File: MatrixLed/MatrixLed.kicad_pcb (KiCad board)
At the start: 2 copper layers, 0 parts

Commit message: Añadida serigrafia reflectante
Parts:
- added C1: 10uF, Capacitors_SMD:C_1206, B.Cu at (205.7, 72.1)
- added D1: LED_ALT, LEDs:LED_0603, F.Cu at (181.0, 59.7)
- added D10: LED_ALT, LEDs:LED_0603, F.Cu at (185.4, 62.9)
- added D11: LED_ALT, LEDs:LED_0603, F.Cu at (185.4, 66.0)
- added D12: LED_ALT, LEDs:LED_0603, F.Cu at (185.4, 69.2)
- added D13: LED_ALT, LEDs:LED_0603, F.Cu at (185.4, 72.4)
- added D14: LED_ALT, LEDs:LED_0603, F.Cu at (185.4, 75.6)
- added D15: LED_ALT, LEDs:LED_0603, F.Cu at (185.4, 78.7)
- added D16: LED_ALT, LEDs:LED_0603, F.Cu at (185.4, 81.9)
- added D17: LED_ALT, LEDs:LED_0603, F.Cu at (189.9, 59.7)
- added D18: LED_ALT, LEDs:LED_0603, F.Cu at (189.9, 62.9)
- added D19: LED_ALT, LEDs:LED_0603, F.Cu at (189.9, 66.0)
- added D2: LED_ALT, LEDs:LED_0603, F.Cu at (181.0, 62.9)
- added D20: LED_ALT, LEDs:LED_0603, F.Cu at (189.9, 69.2)
- added D21: LED_ALT, LEDs:LED_0603, F.Cu at (189.9, 72.4)
- added D22: LED_ALT, LEDs:LED_0603, F.Cu at (189.9, 75.6)
- added D23: LED_ALT, LEDs:LED_0603, F.Cu at (189.9, 78.7)
- added D24: LED_ALT, LEDs:LED_0603, F.Cu at (189.9, 81.9)
- added D25: LED_ALT, LEDs:LED_0603, F.Cu at (194.3, 59.7)
- added D26: LED_ALT, LEDs:LED_0603, F.Cu at (194.3, 62.9)
- added D27: LED_ALT, LEDs:LED_0603, F.Cu at (194.3, 66.0)
- added D28: LED_ALT, LEDs:LED_0603, F.Cu at (194.3, 69.2)
- added D29: LED_ALT, LEDs:LED_0603, F.Cu at (194.3, 72.4)
- added D3: LED_ALT, LEDs:LED_0603, F.Cu at (181.0, 66.0)
- added D30: LED_ALT, LEDs:LED_0603, F.Cu at (194.3, 75.6)
- added D31: LED_ALT, LEDs:LED_0603, F.Cu at (194.3, 78.7)
- added D32: LED_ALT, LEDs:LED_0603, F.Cu at (194.3, 81.9)
- added D33: LED_ALT, LEDs:LED_0603, F.Cu at (198.8, 59.7)
- added D34: LED_ALT, LEDs:LED_0603, F.Cu at (198.8, 62.9)
- added D35: LED_ALT, LEDs:LED_0603, F.Cu at (198.8, 66.0)
- added D36: LED_ALT, LEDs:LED_0603, F.Cu at (198.8, 69.2)
- added D37: LED_ALT, LEDs:LED_0603, F.Cu at (198.8, 72.4)
- added D38: LED_ALT, LEDs:LED_0603, F.Cu at (198.8, 75.6)
- added D39: LED_ALT, LEDs:LED_0603, F.Cu at (198.8, 78.7)
- added D4: LED_ALT, LEDs:LED_0603, F.Cu at (181.0, 69.2)
- added D40: LED_ALT, LEDs:LED_0603, F.Cu at (198.8, 81.9)
- added D41: LED_ALT, LEDs:LED_0603, F.Cu at (203.2, 59.7)
- added D42: LED_ALT, LEDs:LED_0603, F.Cu at (203.2, 62.9)
- added D43: LED_ALT, LEDs:LED_0603, F.Cu at (203.2, 66.0)
- added D44: LED_ALT, LEDs:LED_0603, F.Cu at (203.2, 69.2)
- added D45: LED_ALT, LEDs:LED_0603, F.Cu at (203.2, 72.4)
- added D46: LED_ALT, LEDs:LED_0603, F.Cu at (203.2, 75.6)
- added D47: LED_ALT, LEDs:LED_0603, F.Cu at (203.2, 78.7)
- added D48: LED_ALT, LEDs:LED_0603, F.Cu at (203.2, 81.9)
- added D49: LED_ALT, LEDs:LED_0603, F.Cu at (207.6, 59.7)
- added D5: LED_ALT, LEDs:LED_0603, F.Cu at (181.0, 72.4)
- added D50: LED_ALT, LEDs:LED_0603, F.Cu at (207.6, 62.9)
- added D51: LED_ALT, LEDs:LED_0603, F.Cu at (207.6, 66.0)
- added D52: LED_ALT, LEDs:LED_0603, F.Cu at (207.6, 69.2)
- added D53: LED_ALT, LEDs:LED_0603, F.Cu at (207.6, 72.4)
- added D54: LED_ALT, LEDs:LED_0603, F.Cu at (207.6, 75.6)
- added D55: LED_ALT, LEDs:LED_0603, F.Cu at (207.6, 78.7)
- added D56: LED_ALT, LEDs:LED_0603, F.Cu at (207.6, 81.9)
- added D57: LED_ALT, LEDs:LED_0603, F.Cu at (212.1, 59.7)
- added D58: LED_ALT, LEDs:LED_0603, F.Cu at (212.1, 62.9)
- added D59: LED_ALT, LEDs:LED_0603, F.Cu at (212.1, 66.0)
- added D6: LED_ALT, LEDs:LED_0603, F.Cu at (181.0, 75.6)
- added D60: LED_ALT, LEDs:LED_0603, F.Cu at (212.1, 69.2)
- added D61: LED_ALT, LEDs:LED_0603, F.Cu at (212.1, 72.4)
- added D62: LED_ALT, LEDs:LED_0603, F.Cu at (212.1, 75.6)
- added D63: LED_ALT, LEDs:LED_0603, F.Cu at (212.1, 78.7)
- added D64: LED_ALT, LEDs:LED_0603, F.Cu at (212.1, 81.9)
- added D65: 1N4148, Diodes_SMD:D_SOD-123, B.Cu at (202.5, 72.7)
- added D7: LED_ALT, LEDs:LED_0603, F.Cu at (181.0, 78.7)
- added D8: LED_ALT, LEDs:LED_0603, F.Cu at (181.0, 81.9)
- added D9: LED_ALT, LEDs:LED_0603, F.Cu at (185.4, 59.7)
- added G***: LOGO, logos_frizzy:cuadrado, F.Cu at (212.0, 81.9)
- added G***: LOGO, logos_frizzy:cuadrado, F.Cu at (207.5, 78.9)
- added G***: LOGO, logos_frizzy:cuadrado, F.Cu at (203.1, 78.9)
- added G***: LOGO, logos_frizzy:cuadrado, F.Cu at (198.6, 78.9)
- added G***: LOGO, logos_frizzy:cuadrado, F.Cu at (194.2, 78.9)
- added G***: LOGO, logos_frizzy:cuadrado, F.Cu at (189.7, 78.9)
- added G***: LOGO, logos_frizzy:cuadrado, F.Cu at (185.3, 78.9)
- added G***: LOGO, logos_frizzy:cuadrado, F.Cu at (180.8, 78.9)
- added G***: LOGO, logos_frizzy:cuadrado, F.Cu at (212.0, 75.7)
- added G***: LOGO, logos_frizzy:cuadrado, F.Cu at (207.5, 75.7)
- added G***: LOGO, logos_frizzy:cuadrado, F.Cu at (203.1, 75.7)
- added G***: LOGO, logos_frizzy:cuadrado, F.Cu at (207.5, 81.9)
- added G***: LOGO, logos_frizzy:cuadrado, F.Cu at (198.6, 75.7)
- added G***: LOGO, logos_frizzy:cuadrado, F.Cu at (194.2, 75.7)
- added G***: LOGO, logos_frizzy:cuadrado, F.Cu at (189.7, 75.7)
- added G***: LOGO, logos_frizzy:cuadrado, F.Cu at (185.3, 75.7)
- added G***: LOGO, logos_frizzy:cuadrado, F.Cu at (180.8, 75.7)
- added G***: LOGO, logos_frizzy:cuadrado, F.Cu at (180.8, 72.5)
- added G***: LOGO, logos_frizzy:cuadrado, F.Cu at (185.3, 72.5)
- added G***: LOGO, logos_frizzy:cuadrado, F.Cu at (189.7, 72.5)
- added G***: LOGO, logos_frizzy:cuadrado, F.Cu at (194.2, 72.5)
- added G***: LOGO, logos_frizzy:cuadrado, F.Cu at (198.6, 72.5)
- added G***: LOGO, logos_frizzy:cuadrado, F.Cu at (203.1, 82.0)
- added G***: LOGO, logos_frizzy:cuadrado, F.Cu at (212.0, 72.5)
- added G***: LOGO, logos_frizzy:cuadrado, F.Cu at (212.0, 69.3)
- added G***: LOGO, logos_frizzy:cuadrado, F.Cu at (212.0, 66.2)
- added G***: LOGO, logos_frizzy:cuadrado, F.Cu at (212.0, 63.0)
- added G***: LOGO, logos_frizzy:cuadrado, F.Cu at (212.0, 59.8)
- added G***: LOGO, logos_frizzy:cuadrado, F.Cu at (203.1, 72.5)
- added G***: LOGO, logos_frizzy:cuadrado, F.Cu at (207.5, 72.5)
- added G***: LOGO, logos_frizzy:cuadrado, F.Cu at (207.5, 69.3)
- added G***: LOGO, logos_frizzy:cuadrado, F.Cu at (203.1, 69.3)
- added G***: LOGO, logos_frizzy:cuadrado, F.Cu at (207.5, 59.8)
- added G***: LOGO, logos_frizzy:cuadrado, F.Cu at (198.6, 82.0)
- added G***: LOGO, logos_frizzy:cuadrado, F.Cu at (207.5, 63.0)
- added G***: LOGO, logos_frizzy:cuadrado, F.Cu at (207.5, 66.2)
- added G***: LOGO, logos_frizzy:cuadrado, F.Cu at (203.1, 66.2)
- added G***: LOGO, logos_frizzy:cuadrado, F.Cu at (203.1, 63.0)
- added G***: LOGO, logos_frizzy:cuadrado, F.Cu at (203.1, 59.8)
- added G***: LOGO, logos_frizzy:cuadrado, F.Cu at (198.6, 59.8)
- added G***: LOGO, logos_frizzy:cuadrado, F.Cu at (198.6, 63.0)
- added G***: LOGO, logos_frizzy:cuadrado, F.Cu at (198.6, 66.2)
- added G***: LOGO, logos_frizzy:cuadrado, F.Cu at (198.6, 69.3)
- added G***: LOGO, logos_frizzy:cuadrado, F.Cu at (194.2, 69.3)
- added G***: LOGO, logos_frizzy:cuadrado, F.Cu at (194.2, 82.0)
- added G***: LOGO, logos_frizzy:cuadrado, F.Cu at (194.2, 66.2)
- added G***: LOGO, logos_frizzy:cuadrado, F.Cu at (194.2, 63.0)
- added G***: LOGO, logos_frizzy:cuadrado, F.Cu at (194.2, 59.8)
- added G***: LOGO, logos_frizzy:cuadrado, F.Cu at (189.7, 59.8)
- added G***: LOGO, logos_frizzy:cuadrado, F.Cu at (189.7, 63.0)
- added G***: LOGO, logos_frizzy:cuadrado, F.Cu at (189.7, 66.2)
- added G***: LOGO, logos_frizzy:cuadrado, F.Cu at (189.7, 69.3)
- added G***: LOGO, logos_frizzy:cuadrado, F.Cu at (185.3, 69.3)
- added G***: LOGO, logos_frizzy:cuadrado, F.Cu at (180.8, 69.3)
- added G***: LOGO, logos_frizzy:cuadrado, F.Cu at (185.3, 66.2)
- added G***: LOGO, logos_frizzy:cuadrado, F.Cu at (189.7, 82.0)
- added G***: LOGO, logos_frizzy:cuadrado, F.Cu at (185.3, 63.0)
- added G***: LOGO, logos_frizzy:cuadrado, F.Cu at (185.3, 59.8)
- added G***: LOGO, logos_frizzy:cuadrado, F.Cu at (180.8, 66.2)
- added G***: LOGO, logos_frizzy:cuadrado, F.Cu at (180.8, 63.0)
- added G***: LOGO, logos_frizzy:cuadrado, F.Cu at (180.8, 59.8)
- added G***: LOGO, logos_frizzy:cuadrado, F.Cu at (185.3, 82.0)
- added G***: LOGO, logos_frizzy:cuadrado, F.Cu at (180.8, 82.0)
- added G***: LOGO, logos_frizzy:cuadrado, F.Cu at (212.0, 78.9)
- added JP1: Jumper_NO_Small, Resistors_SMD:R_0805, B.Cu at (181.4, 62.5)
- added JP2: Jumper_NO_Small, Resistors_SMD:R_0805, B.Cu at (209.9, 71.3)
- added JP3: Jumper_NO_Small, Resistors_SMD:R_0805, B.Cu at (211.6, 79.1)
- added P1: CONN_01X04, Connectors_JST:JST_PH_S4B-PH-SM4-TB_04x2.00mm_Angled, F.Cu at (169.9, 70.9)
- added R1: 10K, Resistors_SMD:R_0805, B.Cu at (190.4, 72.9)
- added R2: 10K, Resistors_SMD:R_0805, B.Cu at (193.7, 73.4)
- added R3: 10K, Resistors_SMD:R_0805, B.Cu at (199.4, 72.1)
- added R4: 10K, Resistors_SMD:R_0805, B.Cu at (196.8, 72.1)
- added R5: 10K, Resistors_SMD:R_0805, B.Cu at (208.9, 79.5)
- added U1: HT16K33, Housings_SOIC:SOIC-28W_7.5x17.9mm_Pitch1.27mm, B.Cu at (171.1, 70.9)
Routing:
- net DIG7: track 0.00 -> 42.9 mm, vias 0 -> 8
- net DIG6: track 0.00 -> 42.9 mm, vias 0 -> 8
- net DIG2: track 0.00 -> 42.9 mm, vias 0 -> 8
- net DIG1: track 0.00 -> 42.9 mm, vias 0 -> 8
- net DIG0: track 0.00 -> 42.9 mm, vias 0 -> 8
- net DIG5: track 0.00 -> 42.9 mm, vias 0 -> 8
- net DIG4: track 0.00 -> 34.0 mm, vias 0 -> 7
- net GND: track 0.00 -> 30.5 mm, vias 0 -> 6
- net SEGG: track 0.00 -> 22.2 mm
- net SEGF: track 0.00 -> 22.2 mm
- net SEGE: track 0.00 -> 22.2 mm
- net SEGDP: track 0.00 -> 22.2 mm
- net SEGD: track 0.00 -> 22.2 mm
- net SEGC: track 0.00 -> 22.2 mm
- net SEGB: track 0.00 -> 22.2 mm
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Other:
- board outline added: 49.3 x 26 mm

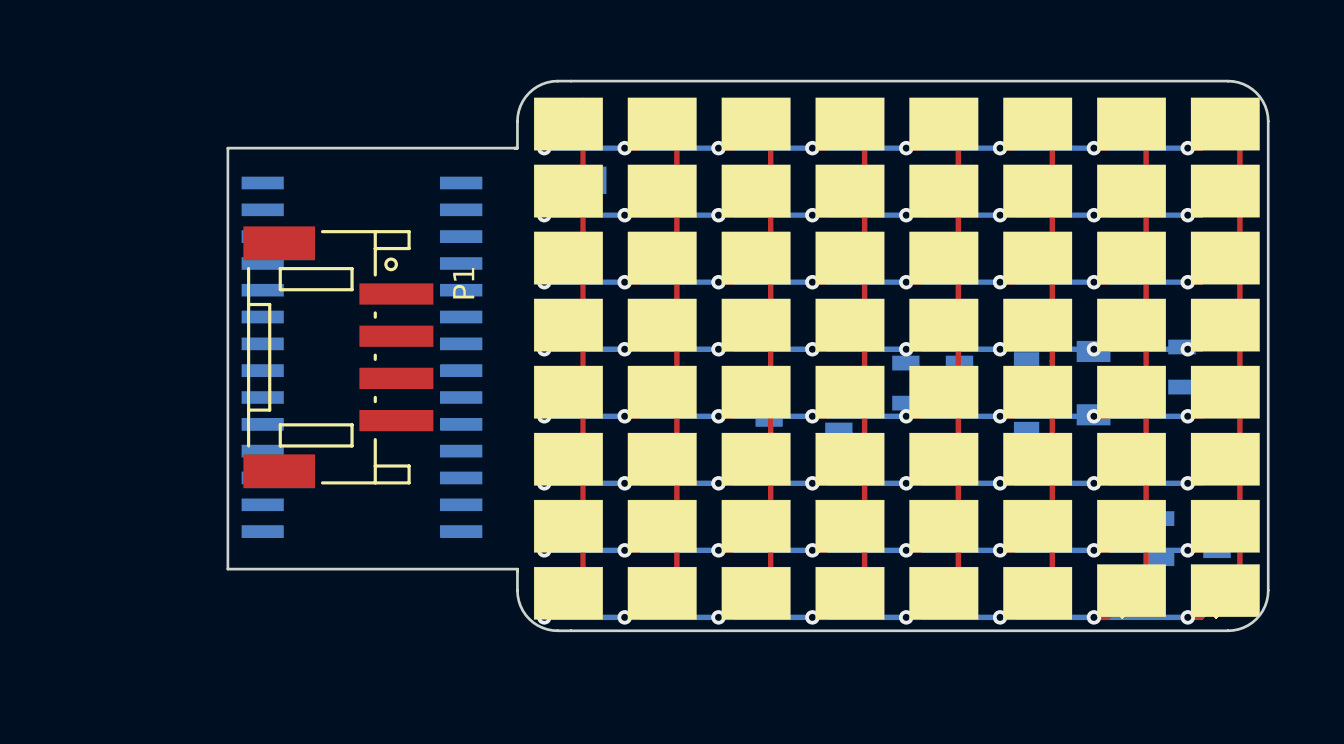
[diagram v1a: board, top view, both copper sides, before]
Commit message: Componentes colocados
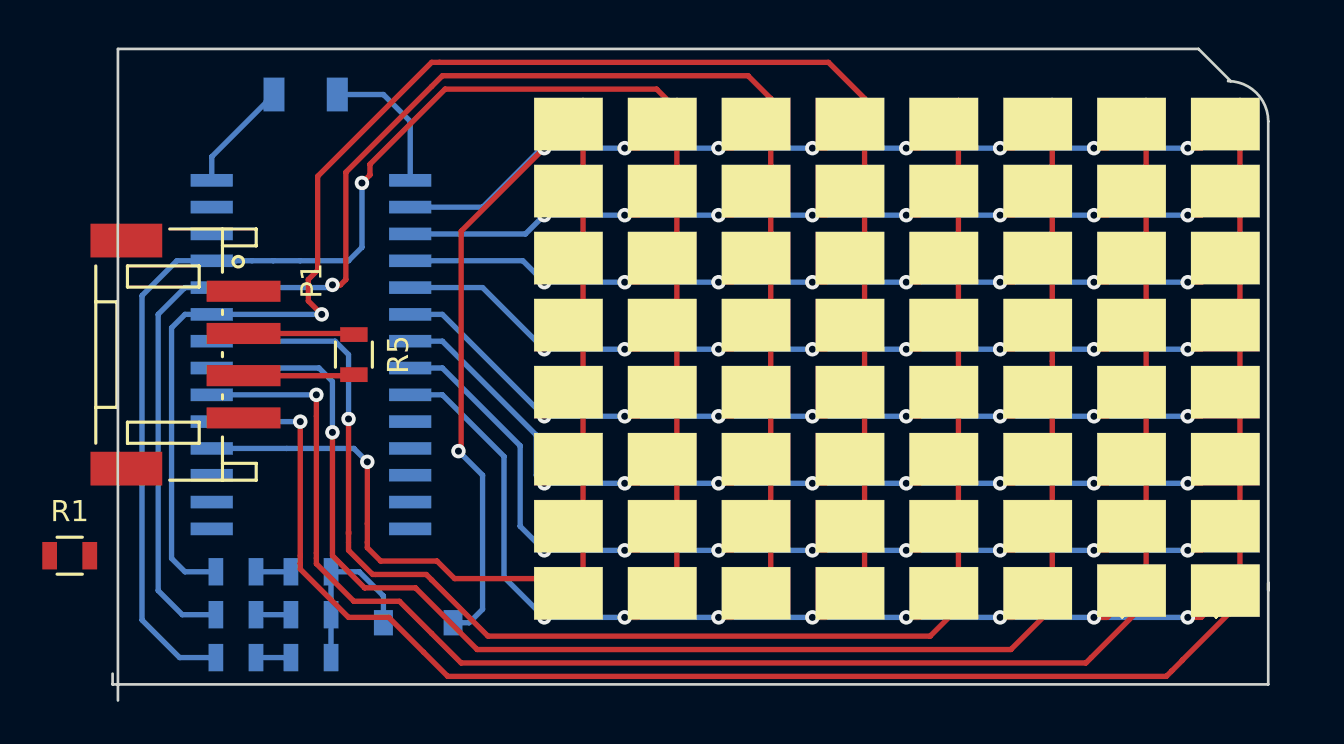
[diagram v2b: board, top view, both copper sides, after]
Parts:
- R1, R5: moved to F.Cu
- moved JP3 46.9 mm to (165.1, 85.1), turned to 0 degrees
- moved JP2 46.3 mm to (165.1, 83.1), turned to 0 degrees
- moved C1 39.7 mm to (168.4, 58.4), turned to 0 degrees
- moved R5 39.2 mm to (170.7, 70.7), turned to 270 degrees
- moved R1 33.9 mm to (157.2, 80.3), turned to 0 degrees
- moved R3 32.6 mm to (168.7, 83.1), turned to 0 degrees
- moved R4 31.0 mm to (168.7, 85.1), turned to 0 degrees
- moved D65 30.7 mm to (173.7, 83.4), turned to 0 degrees
- moved R2 26.2 mm to (168.7, 81.0), turned to 0 degrees
- moved JP1 24.7 mm to (165.1, 81.0)
- moved P1 7.24 mm to (162.7, 70.7)
- moved U1 2.42 mm to (168.7, 70.7), turned to 180 degrees
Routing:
- net SEGG: track 22.2 -> 82.6 mm, vias 0 -> 1
- net SEGC: track 22.2 -> 79.2 mm, vias 0 -> 1
- net SEGF: track 22.2 -> 78.8 mm, vias 0 -> 1
- net SEGB: track 22.2 -> 76.1 mm, vias 0 -> 1
- net SEGE: track 22.2 -> 74.6 mm, vias 0 -> 1
- net SEGA: track 22.2 -> 73.9 mm, vias 0 -> 1
- net SEGD: track 22.2 -> 71.0 mm, vias 0 -> 1
- net DIG3: track 12.4 -> 50.5 mm, vias 1 -> 8
- net DIG0: track 42.9 -> 76.1 mm, vias 8 -> 9
- net GND: track 30.5 -> 7.40 mm, vias 6 -> 0
- net SEGDP: track 22.2 -> 44.7 mm, vias 0 -> 1
- net DIG4: track 34.0 -> 51.2 mm, vias 7 -> 8
- net DIG7: track 42.9 -> 57.0 mm
- net DIG6: track 42.9 -> 55.1 mm
- net DIG5: track 42.9 -> 53.1 mm
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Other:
- board size 49.3 x 26 mm -> 54.7 x 30.9 mm

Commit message: Placa enrutada, taladros realizados y componentes 3D añadidos
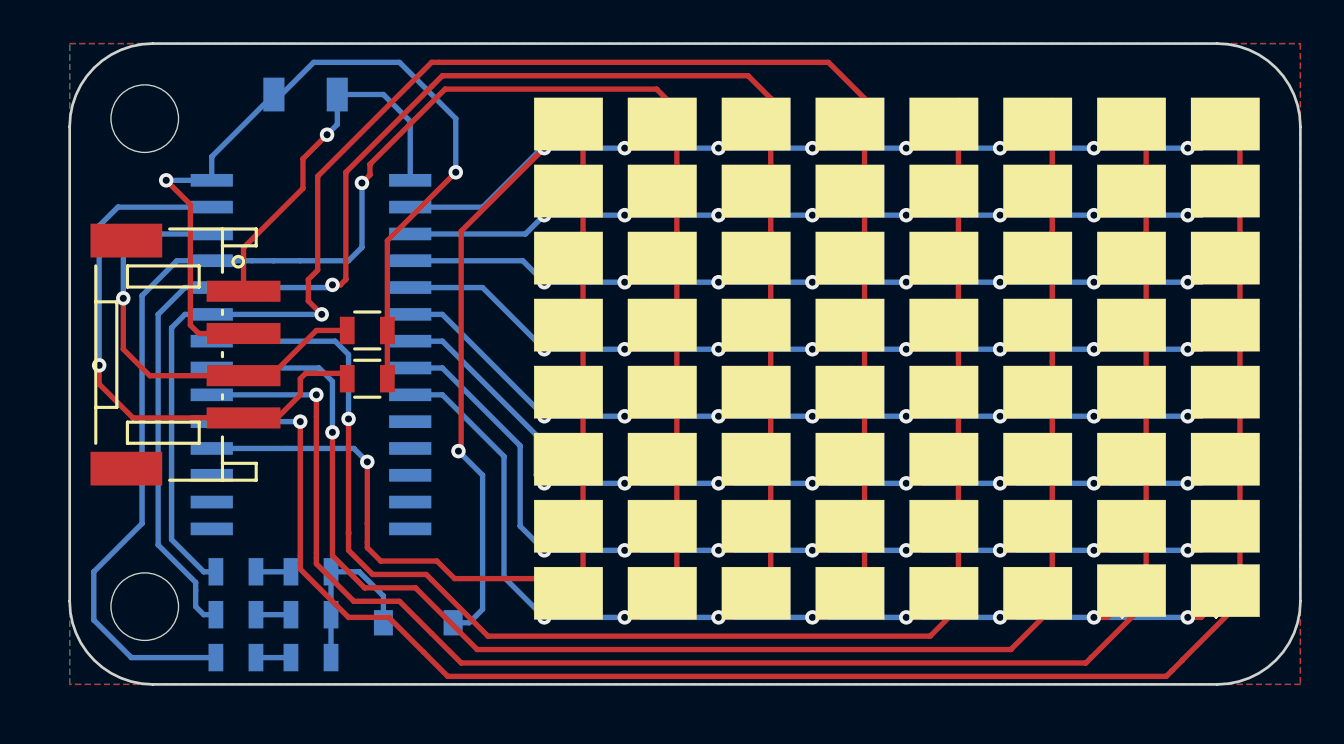
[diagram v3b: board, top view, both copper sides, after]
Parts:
- added REF**: MountingHole_3.2mm_M3, Mounting_Holes:MountingHole_3.2mm_M3, F.Cu at (160.8, 59.6)
- added REF**: MountingHole_3.2mm_M3, Mounting_Holes:MountingHole_3.2mm_M3, F.Cu at (160.8, 82.7)
- moved R1 16.4 mm to (171.3, 71.9), turned to 180 degrees
- moved R5 1.31 mm to (171.3, 69.6), turned to 180 degrees
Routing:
- net VCC: track 10.5 -> 41.5 mm, vias 0 -> 2
- net SDA: track 0.16 -> 27.2 mm, vias 0 -> 1
- net SCL: track 5.25 -> 21.1 mm, vias 0 -> 1
- net GND: track 7.40 -> 18.6 mm, vias 0 -> 1
- net SEGA: track 73.9 -> 77.2 mm
- net SEGC: track 79.2 -> 78.7 mm
- added copper zone on B.Cu, net GND
- added copper zone on F.Cu, net GND
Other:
- board size 54.7 x 30.9 mm -> 58.3 x 30.4 mm

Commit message: Serigrafia añadida
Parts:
- removed the G*** at (189.7, 72.5)
- added G***: LOGO, logos_frizzy:web, B.Cu at (206.8, 71.1)
- added G***: LOGO, logos_frizzy:logo_LM, B.Cu at (191.3, 71.0)
- moved G*** 1.35 mm to (204.0, 71.5)
- turned G*** to 45 degrees
- turned REF** to 45 degrees
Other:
- board text added: "A0"
- board text added: "A1"
- board text added: "A2"

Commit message: DRC pasado y errores solucionados
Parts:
- added G***: LOGO, logos_frizzy:cuadrado, F.Cu at (189.7, 72.5)
- moved G*** 1.27 mm to (203.2, 72.5)
- turned G*** to 180 degrees
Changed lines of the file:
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@@
     (tracks 518)
     (zones 0)
-    (modules 143)
+    (modules 144)
     (nets 33)
   )
@@
     (35 F.Paste user)
     (36 B.SilkS user)
-    (37 F.SilkS user hide)
+    (37 F.SilkS user)
     (38 B.Mask user)
     (39 F.Mask user)
@@
   )
   (module logos_frizzy:cuadrado (layer F.Cu)
+    (at 189.738 72.517)
+    (fp_text reference G*** (at 0 0) (layer F.SilkS) hide
+      (effects (font (thickness 0.3)))
+    )
+    (fp_text value LOGO (at 0.75 0) (layer F.SilkS) hide
+      (effects (font (thickness 0.3)))
+    )
+    (fp_poly (pts (xy 1.628145 1.2446) (xy -1.6256 1.2446) (xy -1.6256 -1.23952) (xy 1.628145 -1.23952)
+      (xy 1.628145 1.2446)) (layer F.SilkS) (width 0.01))
+  )
+  (module logos_frizzy:cuadrado (layer F.Cu)
     (at 211.963 59.817)
     (fp_text reference G*** (at 0 0) (layer F.SilkS) hide
@@
   )
   (module logos_frizzy:cuadrado (layer F.Cu)
-    (at 203.962 71.501)
+    (at 203.2 72.517)
     (fp_text reference G*** (at 0 0) (layer F.SilkS) hide
       (effects (font (thickness 0.3)))
@@
   )
   (module logos_frizzy:cuadrado (layer F.Cu)
-    (at 203.073 69.342 45)
-    (fp_text reference G*** (at 0 0 45) (layer F.SilkS) hide
-      (effects (font (thickness 0.3)))
-    )
-    (fp_text value LOGO (at 0.75 0 45) (layer F.SilkS) hide
-      (effects (font (thickness 0.3)))
-    )
+    (at 203.073 69.342 180)
+    (fp_text reference G*** (at 0 0 180) (layer F.SilkS) hide
+      (effects (font (thickness 0.3)))
+    )
+    (fp_text value LOGO (at 0.75 0 180) (layer F.SilkS) hide
+      (effects (font (thickness 0.3)))
+    )
